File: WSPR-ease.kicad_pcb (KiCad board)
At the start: 4 copper layers, 100 x 75 mm, 98 parts, among them J101 GNSS Ant, J102 USB_C_16P_Stacked, J103 Tx Ant, Q101 MMBF170, Q102 MMBF170, Q103 MMBF170, Q104 MMBF170, Q105 MMBF170, Q106 MMBF170, Q107 MMBF170, Q108 MMBF170, Q109 MMBF170, Q110 MMBF170, Q111 MMBF170, Q112 MMBF170, SW101 BOOTSEL, SW102 RESET, T101 BN-43-202_DualPri_CTSec, U101 W25Q128JVS, U102 RP2040, U103 CD74AC244M, U104 ATGM336H-5N31, U105 NCP1117-3.3_SOT223, Y101 ABM8-272-T3

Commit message: Starting layout a bit
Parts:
- removed AE101: GPS_Patch_25mm, Library:gnss-antenna
- removed Q102, Q103, Q104, Q105, Q106, Q107, Q108, Q109, Q110, Q111, Q112: MMBF170, Package_TO_SOT_SMD:SOT-23
- removed R116, R120: 0, Resistor_SMD:R_0603_1608Metric
- removed R117, R118, R119: 10, Resistor_SMD:R_0603_1608Metric
- removed R121, R122, R125, R126: 100k, Resistor_SMD:R_0603_1608Metric
- removed R123, R124: 5.1k, Resistor_SMD:R_0603_1608Metric
- removed T101: BN-43-202_DualPri_CTSec, Library:bn-43-202-horizontal
- removed U105: NCP1117-3.3_SOT223, Package_TO_SOT_SMD:SOT-223-3_TabPin2
- added C301: 10uF, Capacitor_SMD:C_0805_2012Metric, F.Cu at (115.2, 80.7)
- added C302: 100nF, Capacitor_SMD:C_0603_1608Metric, F.Cu at (112.7, 78.7)
- added C401: 15pF, Capacitor_SMD:C_0603_1608Metric, F.Cu at (116.8, 116.7)
- added C402: 1uF, Capacitor_SMD:C_0603_1608Metric, F.Cu at (109.8, 126.9)
- added C403: 15pF, Capacitor_SMD:C_0603_1608Metric, F.Cu at (116.8, 112.2)
- added C404: 1uF, Capacitor_SMD:C_0603_1608Metric, F.Cu at (114.6, 122.1)
- added C405: 100nF, Capacitor_SMD:C_0603_1608Metric, F.Cu at (114.6, 118.9)
- added C406: 100nF, Capacitor_SMD:C_0603_1608Metric, F.Cu at (106.8, 121.4)
- added C407: 100nF, Capacitor_SMD:C_0603_1608Metric, F.Cu at (115.3, 116.6)
- added C410: 100nF, Capacitor_SMD:C_0603_1608Metric, F.Cu at (103.6, 118.9)
- added C411: 10nF, Capacitor_SMD:C_0603_1608Metric, F.Cu at (110.8, 122.1)
- added C412: 100nF, Capacitor_SMD:C_0603_1608Metric, F.Cu at (102.3, 113.4)
- added C413: 4.7uF, Capacitor_SMD:C_0603_1608Metric, F.Cu at (112.6, 121.7)
- added C414: 100nF, Capacitor_SMD:C_0603_1608Metric, F.Cu at (108.3, 121.4)
- added C417: 100nF, Capacitor_SMD:C_0603_1608Metric, F.Cu at (125.3, 123.7)
- added C418: 6.8nF, Capacitor_SMD:C_0603_1608Metric, F.Cu at (125.3, 119.1)
- added C419: 6.8nF, Capacitor_SMD:C_0603_1608Metric, F.Cu at (125.3, 120.9)
- added FB401: 120 @ 100MHz, Inductor_SMD:L_0805_2012Metric, F.Cu at (109.5, 129.9)
- added J104: Tx Ant, Connector_Coaxial:SMA_BAT_Wireless_BWSMA-KWE-Z001, F.Cu at (143.9, 64.4)
- added J401: RJ45_Hanrun_HR911105A_Horizontal, Connector_RJ:RJ45_Hanrun_HR911105A_Horizontal, F.Cu at (131.6, 126.5)
- added Q301: MMBF170, Package_TO_SOT_SMD:SOT-23, F.Cu at (121.0, 70.6)
- added Q302: MMBF170, Package_TO_SOT_SMD:SOT-23, F.Cu at (124.5, 70.6)
- added Q303: MMBF170, Package_TO_SOT_SMD:SOT-23, F.Cu at (128.0, 70.6)
- added Q304: MMBF170, Package_TO_SOT_SMD:SOT-23, F.Cu at (128.1, 65.5)
- added Q305: MMBF170, Package_TO_SOT_SMD:SOT-23, F.Cu at (124.6, 65.5)
- added Q306: MMBF170, Package_TO_SOT_SMD:SOT-23, F.Cu at (121.1, 65.5)
- added Q307: MMBF170, Package_TO_SOT_SMD:SOT-23, F.Cu at (96.1, 65.3)
- added Q308: MMBF170, Package_TO_SOT_SMD:SOT-23, F.Cu at (92.7, 65.3)
- added Q309: MMBF170, Package_TO_SOT_SMD:SOT-23, F.Cu at (89.1, 65.3)
- added Q310: MMBF170, Package_TO_SOT_SMD:SOT-23, F.Cu at (89.0, 70.5)
- added Q311: MMBF170, Package_TO_SOT_SMD:SOT-23, F.Cu at (92.3, 70.5)
- added Q312: MMBF170, Package_TO_SOT_SMD:SOT-23, F.Cu at (95.8, 70.5)
- added R301: 10, Resistor_SMD:R_0603_1608Metric, F.Cu at (120.0, 74.2)
- added R302: 10, Resistor_SMD:R_0603_1608Metric, F.Cu at (123.5, 74.2)
- added R303: 10, Resistor_SMD:R_0603_1608Metric, F.Cu at (127.0, 74.2)
- added R304: 10, Resistor_SMD:R_0603_1608Metric, F.Cu at (129.1, 61.8)
- added R305: 10, Resistor_SMD:R_0603_1608Metric, F.Cu at (125.6, 61.8)
- added R306: 10, Resistor_SMD:R_0603_1608Metric, F.Cu at (122.1, 61.8)
- added R307: 10, Resistor_SMD:R_0603_1608Metric, F.Cu at (96.8, 61.9)
- added R308: 10, Resistor_SMD:R_0603_1608Metric, F.Cu at (93.6, 61.9)
- added R309: 10, Resistor_SMD:R_0603_1608Metric, F.Cu at (90.1, 61.9)
- added R310: 10, Resistor_SMD:R_0603_1608Metric, F.Cu at (88.1, 74.2)
- added R311: 10, Resistor_SMD:R_0603_1608Metric, F.Cu at (91.6, 74.2)
- added R312: 10, Resistor_SMD:R_0603_1608Metric, F.Cu at (94.8, 74.2)
- added R401: 0, Resistor_SMD:R_0603_1608Metric, F.Cu at (116.0, 114.4)
- added R402: 1M, Resistor_SMD:R_0603_1608Metric, F.Cu at (118.3, 114.5)
- added R403: 10k, Resistor_SMD:R_0603_1608Metric, F.Cu at (117.7, 105.7)
- added R404: 10k, Resistor_SMD:R_0603_1608Metric, F.Cu at (108.7, 105.7)
- added R405: 10k, Resistor_SMD:R_0603_1608Metric, F.Cu at (116.2, 105.7)
- added R406: 10k, Resistor_SMD:R_0603_1608Metric, F.Cu at (114.7, 105.7)
- added R407: 10k, Resistor_SMD:R_0603_1608Metric, F.Cu at (107.1, 105.7)
- added R408: 10k, Resistor_SMD:R_0603_1608Metric, F.Cu at (113.2, 105.7)
- added R409: 10k, Resistor_SMD:R_0603_1608Metric, F.Cu at (105.7, 105.7)
- added R410: 10k, Resistor_SMD:R_0603_1608Metric, F.Cu at (111.7, 105.7)
- added R411: 10k, Resistor_SMD:R_0603_1608Metric, F.Cu at (110.1, 105.7)
- added R412: 12.4k, Resistor_SMD:R_0603_1608Metric, F.Cu at (100.3, 116.4)
- added R413: 3.3, Resistor_SMD:R_0603_1608Metric, F.Cu at (125.5, 126.7)
- added R414: 3.3, Resistor_SMD:R_0603_1608Metric, F.Cu at (122.3, 119.1)
- added R415: 49.9, Resistor_SMD:R_0603_1608Metric, F.Cu at (125.0, 125.2)
- added R416: 49.9, Resistor_SMD:R_0603_1608Metric, F.Cu at (122.0, 117.6)
- added R417: 49.9, Resistor_SMD:R_0603_1608Metric, F.Cu at (125.0, 129.7)
- added R418: 49.9, Resistor_SMD:R_0603_1608Metric, F.Cu at (122.0, 122.4)
- added R419: 3.3, Resistor_SMD:R_0603_1608Metric, F.Cu at (125.5, 128.2)
- added R420: 3.3, Resistor_SMD:R_0603_1608Metric, F.Cu at (122.3, 120.9)
- added R421: 1k, Resistor_SMD:R_0603_1608Metric, F.Cu at (142.6, 131.9)
- added R422: 1k, Resistor_SMD:R_0603_1608Metric, F.Cu at (138.5, 131.9)
- added T301: BN-43-202_DualPri_CTSec, Library:bn-43-202-horizontal, F.Cu at (108.3, 68.4)
- added U301: CD74AC244M, Library:DW20, F.Cu at (107.2, 86.3)
- added U401: LP5907MFX-3.3, Package_TO_SOT_SMD:SOT-23-5, F.Cu at (113.5, 127.8)
- added U402: W5500, Package_QFP:LQFP-48_7x7mm_P0.5mm, F.Cu at (109.1, 114.8)
- added Y401: 25MHz, Crystal:Crystal_SMD_Abracon_ABM8G-4Pin_3.2x2.5mm, F.Cu at (121.0, 114.3)
- C107: footprint Capacitor_SMD:C_0805_2012Metric -> Capacitor_SMD:C_0603_1608Metric
- C110: value 100nF -> 1uF
- C111: value 1uF -> 100nF
- C113, C115: value 100nF -> 10uF; footprint Capacitor_SMD:C_0603_1608Metric -> Capacitor_SMD:C_0805_2012Metric
- C114: footprint Capacitor_SMD:C_0603_1608Metric -> Capacitor_SMD:C_0805_2012Metric
- C116, C120, C122: value 10uF -> 100nF; footprint Capacitor_SMD:C_0805_2012Metric -> Capacitor_SMD:C_0603_1608Metric
- C119: value 100pF NP0 -> 10uF; footprint Capacitor_SMD:C_0603_1608Metric -> Capacitor_SMD:C_0805_2012Metric
- C121: value 100nF -> 100pF NP0
- J101: value GNSS Ant -> DEBUG; footprint Connector_Coaxial:SMA_BAT_Wireless_BWSMA-KWE-Z001 -> Connector:Tag-Connect_TC2030-IDC-NL_2x03_P1.27mm_Vertical
- J102: value USB_C_16P_Stacked -> GNSS Ant; footprint Library:HRO-TYPE-C-31-M-12 -> Connector_Coaxial:SMA_BAT_Wireless_BWSMA-KWE-Z001
- J103: value Tx Ant -> USB_C_16P_Stacked; footprint Connector_Coaxial:SMA_BAT_Wireless_BWSMA-KWE-Z001 -> Library:HRO-TYPE-C-31-M-12
- Q101: value MMBF170 -> 2N7002
- R101, R106: value 10k -> 100k
- R102, R105: value 1k -> 100k
- R103: value 27 -> 10k
- R104: value 27 -> 1k
- R107, R108: value 10 -> 27
- R109: value 10 -> 1k
- R110: value 10 -> 200
- R111: value 10 -> 10k
- R112: value 10 -> 200k
- R113: value 10 -> 100k
- R114, R115: value 10 -> 5.1k
- U103: value CD74AC244M -> NCP1117-3.3_SOT223; footprint Library:DW20 -> Package_TO_SOT_SMD:SOT-223-3_TabPin2
- Y101: value ABM8-272-T3 -> 12MHz
- moved J103 78.2 mm to (49.6, 122.7), turned to 90 degrees
- moved U104 72.0 mm to (67.7, 91.9)
- moved C119 70.5 mm to (55.1, 112.2), turned to 180 degrees
- moved L101 68.0 mm to (59.8, 97.4), turned to 180 degrees
- moved R114 64.9 mm to (57.6, 123.9), turned to 0 degrees
- moved R115 64.5 mm to (57.5, 120.9), turned to 0 degrees
- moved C116 54.9 mm to (79.3, 121.2), turned to 180 degrees
- moved BT101 53.5 mm to (75.8, 89.8), turned to -90 degrees
- moved C107 49.5 mm to (89.6, 132.7), turned to 180 degrees
- moved R113 49.5 mm to (71.6, 113.9), turned to -90 degrees
- moved C203 49.2 mm to (144.9, 86.4), turned to 0 degrees
- moved R106 49.2 mm to (86.1, 131.4), turned to -90 degrees
- moved C211 47.9 mm to (147.8, 80.7), turned to -90 degrees
- moved S201 46.2 mm to (136.9, 90.9), turned to -90 degrees
- moved L203 46.1 mm to (144.2, 83.9), turned to 90 degrees
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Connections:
- C107 pad 1: GND -> +3.3V
- C107 pad 2: +3.3V -> GND
- C109 pad 1: GND -> +3.3V
- C109 pad 2: +3.3V -> GND
- C110 pad 1: +3.3V -> Net-(U102-VREG_IN)
- C114 pad 1: +3.3V -> Net-(Q101-S)
- C115 pad 1: +3.3V -> VBUS
- C119 pad 1: Net-(C119-Pad1) -> +3.3V
- C119 pad 2: Net-(J101-In) -> GND
- C120 pad 1: VBUS -> +3.3V
- C121 pad 1: VBUS -> Net-(U104-RF_IN)
- C121 pad 2: GND -> Net-(J102-In)
- C123 pad 1: +3.3V -> VBUS
- J101 pad 1: Net-(J101-In) -> +3.3V
- J101 pad 2: GND -> /SWD
- L101 pad 2: Net-(J101-In) -> Net-(J102-In)
- Q101 pad 1: Net-(Q101-G) -> +3.3V
- Q101 pad 2: GND -> Net-(Q101-S)
- R101 pad 1: +3.3V -> /hiON
- R101 pad 2: Net-(U102-RUN) -> GND
- R102 pad 1: Net-(R102-Pad1) -> /loON
- R102 pad 2: /qsSS -> GND
- R103 pad 1: /D+ -> +3.3V
- R103 pad 2: Net-(U102-USB_DP) -> /nRESET
- R104 pad 1: /D- -> Net-(R104-Pad1)
- R104 pad 2: Net-(U102-USB_DM) -> /qsSS
- R105 pad 1: Net-(C102-Pad2) -> /lo1ON
- R105 pad 2: Net-(U102-XOUT) -> GND
- R106 pad 1: Net-(U102-GPIO14) -> /lo2ON
- R106 pad 2: /gnssPPS -> GND
- R107 pad 1: Net-(U103-1Y0) -> /D+
- R107 pad 2: Net-(Q101-G) -> Net-(U102-USB_DP)
- R108 pad 1: Net-(U103-1Y0) -> /D-
- R108 pad 2: Net-(Q102-G) -> Net-(U102-USB_DM)
- R109 pad 1: Net-(U103-1Y0) -> Net-(C102-Pad2)
- R109 pad 2: Net-(Q103-G) -> Net-(U102-XOUT)
- R110 pad 1: Net-(U103-1Y2) -> +3.3V
- R110 pad 2: Net-(Q104-G) -> Net-(U102-ADC_AVDD)
- R111 pad 1: Net-(U103-1Y2) -> Net-(U102-GPIO14)
- R111 pad 2: Net-(Q105-G) -> /gnssPPS
- R112 pad 1: Net-(U103-1Y2) -> VBUS
- R112 pad 2: Net-(Q106-G) -> Net-(Q101-S)
- R113 pad 1: Net-(U103-2Y0) -> Net-(Q101-S)
- R113 pad 2: Net-(Q107-G) -> GND
- R114 pad 1: Net-(U103-2Y0) -> Net-(J103-CC1)
- R114 pad 2: Net-(Q108-G) -> GND
- R115 pad 1: Net-(U103-2Y0) -> Net-(J103-CC2)
- R115 pad 2: Net-(Q109-G) -> GND
- SW101 pad 2: Net-(R102-Pad1) -> Net-(R104-Pad1)
- SW102 pad 2: Net-(U102-RUN) -> /nRESET
- U102 pad 24: unconnected-(U102-SWCLK-Pad24) -> /SWCLK
- U102 pad 25: unconnected-(U102-SWD-Pad25) -> /SWD
- U102 pad 26: Net-(U102-RUN) -> /nRESET
- U102 pad 27: unconnected-(U102-GPIO16-Pad27) -> /ethMISO
- U102 pad 28: unconnected-(U102-GPIO17-Pad28) -> /ethNCS
- U102 pad 29: unconnected-(U102-GPIO18-Pad29) -> /ethSCLK
- U102 pad 30: unconnected-(U102-GPIO19-Pad30) -> /ethMOSI
- U102 pad 31: unconnected-(U102-GPIO20-Pad31) -> /ethNIRQ
- U102 pad 32: unconnected-(U102-GPIO21-Pad32) -> /ethRESET
- U102 pad 41: unconnected-(U102-GPIO29_ADC3-Pad41) -> Net-(Q101-D)
- U102 pad 43: +3.3V -> Net-(U102-ADC_AVDD)
- U102 pad 44: +3.3V -> Net-(U102-VREG_IN)
- U103 pad 2: /push1 -> +3.3V
- U103 pad 3: Net-(U103-2Y2) -> VBUS
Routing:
- added copper zone on In2.Cu, net +3.3V
- added copper zone on In1.Cu, net GND
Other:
- board text added: "*"

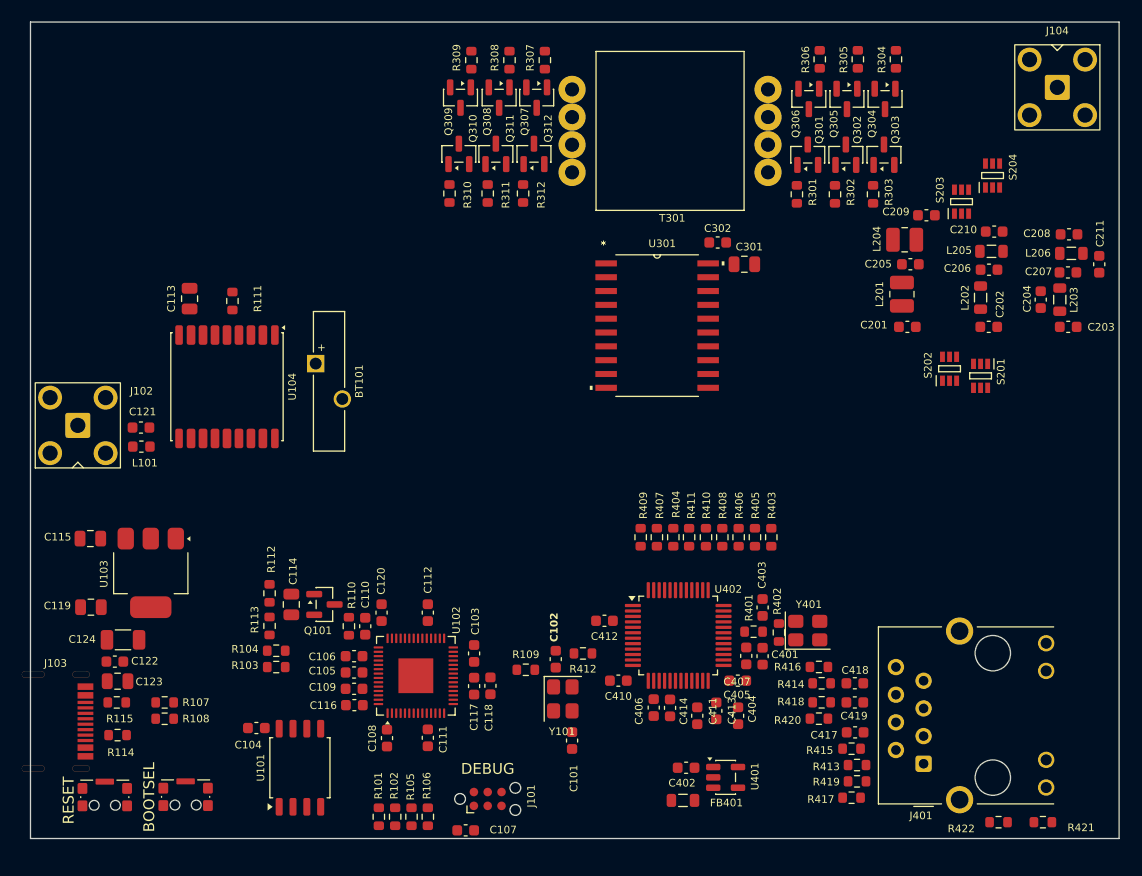
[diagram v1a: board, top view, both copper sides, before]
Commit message: Well it is routed and passes DRC
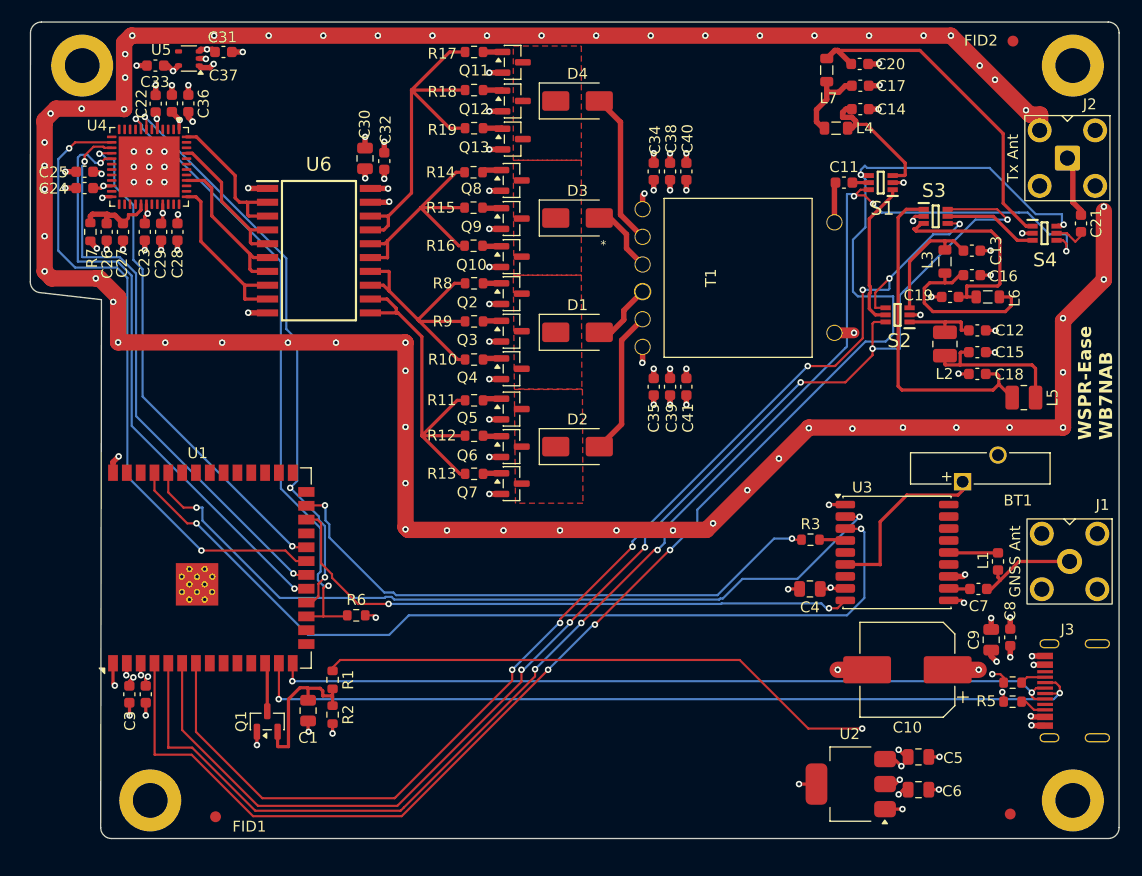
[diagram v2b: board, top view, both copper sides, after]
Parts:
- removed BT101: CR1220, Battery:Battery_Panasonic_CR1220-VCN_Vertical_CircularHoles
- removed C101, C102, C208: 15pF NP0, Capacitor_SMD:C_0603_1608Metric
- removed C103, C104, C105, C108, C109, C111, C112, C116, C117, C118, C120, C122, C302, C405, C406, C407, C410, C412, C414, C417: 100nF, Capacitor_SMD:C_0603_1608Metric
- removed C106, C110, C402, C404: 1uF, Capacitor_SMD:C_0603_1608Metric
- removed C107: 10uF, Capacitor_SMD:C_0603_1608Metric
- removed C113, C115, C119, C123, C301: 10uF, Capacitor_SMD:C_0805_2012Metric
- removed C114: 100nF, Capacitor_SMD:C_0805_2012Metric
- removed C121: 100pF NP0, Capacitor_SMD:C_0603_1608Metric
- removed C124: 100uF, Capacitor_SMD:C_1206_3216Metric
- removed C201, C209: 1nF NP0, Capacitor_SMD:C_0603_1608Metric
- removed C202, C210: 330pF NP0, Capacitor_SMD:C_0603_1608Metric
- removed C203, C211: 120pF NP0, Capacitor_SMD:C_0603_1608Metric
- removed C204: 33pF NP0, Capacitor_SMD:C_0603_1608Metric
- removed C205: 1.8nF NP0, Capacitor_SMD:C_0603_1608Metric
- removed C206: 560pF NP0, Capacitor_SMD:C_0603_1608Metric
- removed C207: 270pF NP0, Capacitor_SMD:C_0603_1608Metric
- removed C401, C403: 15pF, Capacitor_SMD:C_0603_1608Metric
- removed C411: 10nF, Capacitor_SMD:C_0603_1608Metric
- removed C413: 4.7uF, Capacitor_SMD:C_0603_1608Metric
- removed C418, C419: 6.8nF, Capacitor_SMD:C_0603_1608Metric
- removed FB401: 120 @ 100MHz, Inductor_SMD:L_0805_2012Metric
- removed J101: DEBUG, Connector:Tag-Connect_TC2030-IDC-NL_2x03_P1.27mm_Vertical
- removed J102: GNSS Ant, Connector_Coaxial:SMA_BAT_Wireless_BWSMA-KWE-Z001
- removed J103: USB_C_16P_Stacked, Library:HRO-TYPE-C-31-M-12
- removed J104: Tx Ant, Connector_Coaxial:SMA_BAT_Wireless_BWSMA-KWE-Z001
- removed J401: RJ45_Hanrun_HR911105A_Horizontal, Connector_RJ:RJ45_Hanrun_HR911105A_Horizontal
- removed L101: 47nH, Inductor_SMD:L_0603_1608Metric
- removed L201, L204: 2.2uH, Inductor_SMD:L_1008_2520Metric
- removed L202, L205: 390nH, Inductor_SMD:L_0805_2012Metric
- removed L203, L206: 270nH, Inductor_SMD:L_0805_2012Metric
- removed Q101: 2N7002, Package_TO_SOT_SMD:SOT-23
- removed Q301, Q302, Q303, Q304, Q305, Q306, Q307, Q308, Q309, Q310, Q311, Q312: MMBF170, Package_TO_SOT_SMD:SOT-23
- removed R101, R102, R105, R106, R113: 100k, Resistor_SMD:R_0603_1608Metric
- removed R103, R111, R403, R404, R405, R406, R407, R408, R409, R410, R411: 10k, Resistor_SMD:R_0603_1608Metric
- removed R104, R109, R421, R422: 1k, Resistor_SMD:R_0603_1608Metric
- removed R107, R108: 27, Resistor_SMD:R_0603_1608Metric
- removed R110: 200, Resistor_SMD:R_0603_1608Metric
- removed R112: 200k, Resistor_SMD:R_0603_1608Metric
- removed R114, R115: 5.1k, Resistor_SMD:R_0603_1608Metric
- removed R301, R302, R303, R304, R305, R306, R307, R308, R309, R310, R311, R312: 10, Resistor_SMD:R_0603_1608Metric
- removed R401: 0, Resistor_SMD:R_0603_1608Metric
- removed R402: 1M, Resistor_SMD:R_0603_1608Metric
- removed R412: 12.4k, Resistor_SMD:R_0603_1608Metric
- removed R413, R414, R419, R420: 3.3, Resistor_SMD:R_0603_1608Metric
- removed R415, R416, R417, R418: 49.9, Resistor_SMD:R_0603_1608Metric
- removed S201, S202, S203, S204: AS183-92LF, Library:SOT65P220X110-6N
- removed SW101: BOOTSEL, Button_Switch_SMD:SW_SPST_CK_KMS2xxGP
- removed SW102: RESET, Button_Switch_SMD:SW_SPST_CK_KMS2xxGP
- removed T301: BN-43-202_DualPri_CTSec, Library:bn-43-202-horizontal
- removed U101: W25Q128JVS, Package_SO:SOIC-8_5.3x5.3mm_P1.27mm
- removed U102: RP2040, Package_DFN_QFN:QFN-56-1EP_7x7mm_P0.4mm_EP3.2x3.2mm
- removed U103: NCP1117-3.3_SOT223, Package_TO_SOT_SMD:SOT-223-3_TabPin2
- removed U104: ATGM336H-5N31, RF_GPS:ublox_MAX
- removed U301: CD74AC244M, Library:DW20
- removed U401: LP5907MFX-3.3, Package_TO_SOT_SMD:SOT-23-5
- removed U402: W5500, Package_QFP:LQFP-48_7x7mm_P0.5mm
- removed Y101: 12MHz, Crystal:Crystal_SMD_Abracon_ABM8G-4Pin_3.2x2.5mm
- removed Y401: 25MHz, Crystal:Crystal_SMD_Abracon_ABM8G-4Pin_3.2x2.5mm
- added BT1: CR1220, Battery:Battery_Panasonic_CR1220-VCN_Vertical_CircularHoles, F.Cu at (135.2, 100.6)
- added C1: 100nF, Capacitor_SMD:C_0805_2012Metric, F.Cu at (75.1, 121.7)
- added C10: 100uF, Capacitor_SMD:CP_Elec_8x10.5, F.Cu at (130.2, 117.9)
- added C11: 100nF, Capacitor_SMD:C_0603_1608Metric, F.Cu at (124.3, 73.2)
- added C12: 470pF, Capacitor_SMD:C_0603_1608Metric, F.Cu at (136.6, 86.7)
- added C13: 220pF, Capacitor_SMD:C_0603_1608Metric, F.Cu at (136.1, 79.4)
- added C14: 100pF, Capacitor_SMD:C_0603_1608Metric, F.Cu at (125.8, 66.4)
- added C15: 1nF, Capacitor_SMD:C_0603_1608Metric, F.Cu at (136.6, 88.7)
- added C16: 470pF, Capacitor_SMD:C_0603_1608Metric, F.Cu at (136.1, 81.7)
- added C17: 220pF, Capacitor_SMD:C_0603_1608Metric, F.Cu at (125.8, 64.2)
- added C18: 470pF, Capacitor_SMD:C_0603_1608Metric, F.Cu at (136.6, 90.7)
- added C19: 220pF, Capacitor_SMD:C_0603_1608Metric, F.Cu at (134.1, 83.7)
- added C2: 0.1uF, Capacitor_SMD:C_0603_1608Metric, F.Cu at (60.2, 120.2)
- added C20: 100pF, Capacitor_SMD:C_0603_1608Metric, F.Cu at (125.8, 62.2)
- added C21: 100nF, Capacitor_SMD:C_0603_1608Metric, F.Cu at (146.1, 76.9)
- added C22: 0.1uF, Capacitor_SMD:C_0603_1608Metric, F.Cu at (61.1, 65.9)
- added C23: 10uF, Capacitor_SMD:C_0603_1608Metric, F.Cu at (60.1, 77.7)
- added C24: 0.1uF, Capacitor_SMD:C_0603_1608Metric, F.Cu at (54.6, 73.7)
- added C25: 10uF, Capacitor_SMD:C_0603_1608Metric, F.Cu at (54.6, 72.2)
- added C26: 0.1uF, Capacitor_SMD:C_0603_1608Metric, F.Cu at (56.6, 77.7)
- added C27: 10uF, Capacitor_SMD:C_0603_1608Metric, F.Cu at (58.1, 77.7)
- added C28: 0.1uF, Capacitor_SMD:C_0603_1608Metric, F.Cu at (63.1, 77.7)
- added C29: 10uF, Capacitor_SMD:C_0603_1608Metric, F.Cu at (61.6, 77.7)
- added C3: 22uF, Capacitor_SMD:C_0603_1608Metric, F.Cu at (58.7, 120.2)
- added C30: 10uF, Capacitor_SMD:C_0805_2012Metric, F.Cu at (80.3, 70.9)
- added C31: 1uF, Capacitor_SMD:C_0603_1608Metric, F.Cu at (67.3, 61.1)
- added C32: 0.1uF, Capacitor_SMD:C_0603_1608Metric, F.Cu at (82.1, 71.2)
- added C33: 1uF, Capacitor_SMD:C_0603_1608Metric, F.Cu at (61.1, 62.4)
- added C34: 10uF X7R, Capacitor_SMD:C_0603_1608Metric, F.Cu at (106.8, 72.1)
- added C35: 10uF X7R, Capacitor_SMD:C_0603_1608Metric, F.Cu at (106.8, 91.9)
- added C36: 0.1uF, Capacitor_SMD:C_0603_1608Metric, F.Cu at (64.1, 65.9)
- added C37: 10uF, Capacitor_SMD:C_0603_1608Metric, F.Cu at (62.6, 65.9)
- added C38: 0.1uF X7R, Capacitor_SMD:C_0603_1608Metric, F.Cu at (108.3, 72.1)
- added C39: 0.1uF X7R, Capacitor_SMD:C_0603_1608Metric, F.Cu at (108.3, 91.9)
- added C4: 10uF, Capacitor_SMD:C_0805_2012Metric, F.Cu at (121.2, 110.5)
- added C40: 100pF NP0 50V, Capacitor_SMD:C_0603_1608Metric, F.Cu at (109.8, 72.1)
- added C41: 100pF NP0 50V, Capacitor_SMD:C_0603_1608Metric, F.Cu at (109.8, 91.9)
- added C5: 10uF, Capacitor_SMD:C_0805_2012Metric, F.Cu at (131.2, 125.9)
- added C6: 10uF, Capacitor_SMD:C_0805_2012Metric, F.Cu at (131.2, 128.9)
- added C7: 100pF NP0, Capacitor_SMD:C_0603_1608Metric, F.Cu at (136.7, 110.5)
- added C8: 100nF, Capacitor_SMD:C_0603_1608Metric, F.Cu at (139.6, 114.9)
- added C9: 10uF, Capacitor_SMD:C_0805_2012Metric, F.Cu at (137.8, 115.1)
- added D1: SS14, Diode_SMD:D_SMA, F.Cu at (99.8, 86.9)
- added D2: SS14, Diode_SMD:D_SMA, F.Cu at (99.8, 97.4)
- added D3: SS14, Diode_SMD:D_SMA, F.Cu at (99.8, 76.4)
- added D4: SS14, Diode_SMD:D_SMA, F.Cu at (99.8, 65.7)
- added FID1: Fiducial, Fiducial:Fiducial_1mm_Mask2mm, F.Cu at (66.6, 131.4)
- added FID2: Fiducial, Fiducial:Fiducial_1mm_Mask2mm, F.Cu at (139.8, 60.1)
- added FID3: Fiducial, Fiducial:Fiducial_1mm_Mask2mm, F.Cu at (139.6, 131.2)
- added H1: MountingHole_Pad, MountingHole:MountingHole_3.2mm_M3_ISO7380_Pad, F.Cu at (60.6, 129.9)
- added H2: MountingHole_Pad, MountingHole:MountingHole_3.2mm_M3_ISO7380_Pad, F.Cu at (145.3, 62.4)
- added H3: MountingHole_Pad, MountingHole:MountingHole_3.2mm_M3_ISO7380_Pad, F.Cu at (54.4, 62.4)
- added H4: MountingHole_Pad, MountingHole:MountingHole_3.2mm_M3_ISO7380_Pad, F.Cu at (145.3, 129.9)
- added J1: GNSS Ant, Connector_Coaxial:SMA_BAT_Wireless_BWSMA-KWE-Z001, F.Cu at (145.1, 108.0)
- added J2: Tx Ant, Connector_Coaxial:SMA_BAT_Wireless_BWSMA-KWE-Z001, F.Cu at (144.8, 70.9)
- added J3: USB_C_16P_Stacked, Library:HRO-TYPE-C-31-M-12, F.Cu at (147.8, 119.8)
- added L1: 47nH, Inductor_SMD:L_0603_1608Metric, F.Cu at (138.5, 108.0)
- added L2: 1.2uH, Inductor_SMD:L_1008_2520Metric, F.Cu at (133.6, 88.0)
- added L3: 560nH, Inductor_SMD:L_0805_2012Metric, F.Cu at (133.6, 80.4)
- added L4: 270nH, Inductor_SMD:L_0805_2012Metric, F.Cu at (123.6, 68.2)
- added L5: 1.2uH, Inductor_SMD:L_1008_2520Metric, F.Cu at (140.8, 92.9)
- added L6: 560nH, Inductor_SMD:L_0805_2012Metric, F.Cu at (137.5, 83.7)
- added L7: 270nH, Inductor_SMD:L_0805_2012Metric, F.Cu at (122.7, 62.8)
- added Q1: MMBF170, Package_TO_SOT_SMD:SOT-23, F.Cu at (71.3, 122.7)
- added Q10: MMBF170, Package_TO_SOT_SMD:SOT-23, F.Cu at (93.8, 80.0)
- added Q11: MMBF170, Package_TO_SOT_SMD:SOT-23, F.Cu at (93.9, 62.1)
- added Q12: MMBF170, Package_TO_SOT_SMD:SOT-23, F.Cu at (93.9, 65.7)
- added Q13: MMBF170, Package_TO_SOT_SMD:SOT-23, F.Cu at (93.9, 69.2)
- added Q2: MMBF170, Package_TO_SOT_SMD:SOT-23, F.Cu at (93.8, 83.3)
- added Q3: MMBF170, Package_TO_SOT_SMD:SOT-23, F.Cu at (93.8, 86.8)
- added Q4: MMBF170, Package_TO_SOT_SMD:SOT-23, F.Cu at (93.8, 90.2)
- added Q5: MMBF170, Package_TO_SOT_SMD:SOT-23, F.Cu at (93.8, 94.0)
- added Q6: MMBF170, Package_TO_SOT_SMD:SOT-23, F.Cu at (93.8, 97.4)
- added Q7: MMBF170, Package_TO_SOT_SMD:SOT-23, F.Cu at (93.8, 100.8)
- added Q8: MMBF170, Package_TO_SOT_SMD:SOT-23, F.Cu at (93.8, 73.0)
- added Q9: MMBF170, Package_TO_SOT_SMD:SOT-23, F.Cu at (93.8, 76.5)
- added R1: 100k, Resistor_SMD:R_0603_1608Metric, F.Cu at (77.3, 118.8)
- added R10: 10, Resistor_SMD:R_0603_1608Metric, F.Cu at (90.3, 89.4)
- added R11: 10, Resistor_SMD:R_0603_1608Metric, F.Cu at (90.3, 93.2)
- added R12: 10, Resistor_SMD:R_0603_1608Metric, F.Cu at (90.3, 96.4)
- added R13: 10, Resistor_SMD:R_0603_1608Metric, F.Cu at (90.3, 99.9)
- added R14: 10, Resistor_SMD:R_0603_1608Metric, F.Cu at (90.3, 72.2)
- added R15: 10, Resistor_SMD:R_0603_1608Metric, F.Cu at (90.3, 75.5)
- added R16: 10, Resistor_SMD:R_0603_1608Metric, F.Cu at (90.3, 79.0)
- added R17: 10, Resistor_SMD:R_0603_1608Metric, F.Cu at (90.3, 61.1)
- added R18: 10, Resistor_SMD:R_0603_1608Metric, F.Cu at (90.3, 64.7)
- added R19: 10, Resistor_SMD:R_0603_1608Metric, F.Cu at (90.3, 68.2)
- added R2: 100k, Resistor_SMD:R_0603_1608Metric, F.Cu at (77.3, 122.0)
- added R3: 10k, Resistor_SMD:R_0603_1608Metric, F.Cu at (121.2, 106.0)
- added R4: 5.1k, Resistor_SMD:R_0603_1608Metric, F.Cu at (139.8, 119.1)
- added R5: 5.1k, Resistor_SMD:R_0603_1608Metric, F.Cu at (139.8, 120.8)
- added R6: 10k, Resistor_SMD:R_0603_1608Metric, F.Cu at (79.5, 112.9)
- added R7: 10, Resistor_SMD:R_0603_1608Metric, F.Cu at (55.1, 77.7)
- added R8: 10, Resistor_SMD:R_0603_1608Metric, F.Cu at (90.3, 82.4)
- added R9: 10, Resistor_SMD:R_0603_1608Metric, F.Cu at (90.3, 85.9)
- added S1: AS183-92LF, Library:SOT65P220X110-6N, F.Cu at (127.7, 73.2)
- added S2: AS183-92LF, Library:SOT65P220X110-6N, F.Cu at (129.2, 85.3)
- added S3: AS183-92LF, Library:SOT65P220X110-6N, F.Cu at (132.8, 76.2)
- added S4: AS183-92LF, Library:SOT65P220X110-6N, F.Cu at (142.8, 77.8)
- added T1: BN-43-202_DualPri_CTSec, Library:bn-43-202-horizontal, F.Cu at (114.6, 81.9)
- added U1: ESP32-S3-WROOM-1, Library:ESP32-S3-WROOM-1, F.Cu at (62.4, 108.5)
- added U2: NCP1117-3.3_SOT223, Package_TO_SOT_SMD:SOT-223-3_TabPin2, F.Cu at (125.0, 128.4)
- added U3: ATGM336H-5N31, RF_GPS:ublox_MAX, F.Cu at (129.2, 107.1)
- added U4: ICE40UP5K-SG48ITR, Package_DFN_QFN:QFN-48-1EP_7x7mm_P0.5mm_EP5.6x5.6mm, F.Cu at (60.5, 71.7)
- added U5: TLV70012, Package_TO_SOT_SMD:SOT-353_SC-70-5, F.Cu at (64.2, 61.8)
- added U6: CD74ACT541M96G4, Library:SOIC127P1030X265-20N, F.Cu at (76.1, 79.4)
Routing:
- net GND: track 0.00 -> 338.3 mm, vias 0 -> 139
- net /hiON: track 0.00 -> 139.9 mm, vias 0 -> 5
- net /loON: track 0.00 -> 132.1 mm, vias 0 -> 6
- net /lo1ON: track 0.00 -> 121.0 mm, vias 0 -> 6
- net /lo2ON: track 0.00 -> 110.6 mm, vias 0 -> 7
- net /gnssRx: track 0.00 -> 81.7 mm, vias 0 -> 2
- net /D-: track 0.00 -> 78.8 mm, vias 0 -> 2
- net /gnssTx: track 0.00 -> 74.6 mm, vias 0 -> 2
- net VBUS: track 0.00 -> 74.2 mm, vias 0 -> 18
- net /D+: track 0.00 -> 73.1 mm, vias 0 -> 2
- net /fpgaNRESET: track 0.00 -> 59.9 mm, vias 0 -> 2
- net /fpgaMISO: track 0.00 -> 59.2 mm, vias 0 -> 2
- net /gnssNRESET: track 0.00 -> 55.6 mm, vias 0 -> 2
- net /fpgaMOSI: track 0.00 -> 54.8 mm, vias 0 -> 2
- net /fpgaDONE: track 0.00 -> 54.4 mm, vias 0 -> 3
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- added copper zone on In2.Cu, net +1V2
- added copper zone on F.Cu, net /Transmitter/pull1D
- added copper zone on F.Cu, net /Transmitter/pull2D
- added copper zone on F.Cu, net /Transmitter/push1D
- added copper zone on F.Cu, net /Transmitter/push2D
- added copper zone on In2.Cu, net VBUS
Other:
- outline, holes or cut-outs redrawn
- board text added: "WSPR-Ease WB7NAB"

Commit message: Minor tweaks after submitting 001 build to pcbway
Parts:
- added R20: 10k, Resistor_SMD:R_0603_1608Metric, F.Cu at (67.3, 77.4)
- added R21: 10k, Resistor_SMD:R_0603_1608Metric, F.Cu at (70.8, 68.9)
- added R22: 10k, Resistor_SMD:R_0603_1608Metric, F.Cu at (65.8, 80.7)
- added R23: 10k, Resistor_SMD:R_0603_1608Metric, F.Cu at (65.8, 83.9)
- BT1: value CR1220 -> S8401-46; footprint Battery:Battery_Panasonic_CR1220-VCN_Vertical_CircularHoles -> Library:S8401-46
- C1: footprint Capacitor_SMD:C_0805_2012Metric -> Capacitor_SMD:C_0603_1608Metric
- moved BT1 39.5 mm to (105.8, 127.0), turned to 180 degrees
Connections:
- net Net-(D1-A) renamed /Transmitter/push1T
- net Net-(D2-A) renamed /Transmitter/push2T
- net Net-(D3-A) renamed /Transmitter/pull1T
- net Net-(D4-A) renamed /Transmitter/pull2T
- BT1 pad 1: Net-(BT1-+) -> GND
- BT1 pad 2: GND -> Net-(U3-V_BCKP)
- D3 pad 1: /Transmitter/pull2D -> /Transmitter/pull1D
- D4 pad 1: /Transmitter/pull1D -> /Transmitter/pull2D
- Q10 pad 3: /Transmitter/pull2D -> /Transmitter/pull1D
- Q11 pad 3: /Transmitter/pull1D -> /Transmitter/pull2D
- Q12 pad 3: /Transmitter/pull1D -> /Transmitter/pull2D
- Q13 pad 3: /Transmitter/pull1D -> /Transmitter/pull2D
- Q8 pad 3: /Transmitter/pull2D -> /Transmitter/pull1D
- Q9 pad 3: /Transmitter/pull2D -> /Transmitter/pull1D
- U3 pad 6: Net-(BT1-+) -> Net-(U3-V_BCKP)
- U4 pad 40: /Transmitter/push1 -> unconnected-(U4A-RGB1-Pad40)
- U4 pad 42: unconnected-(U4A-IOT_51a-Pad42) -> /Transmitter/push1
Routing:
- net Net-(U3-V_BCKP): track 0.00 -> 38.7 mm, vias 0 -> 2
- net Net-(BT1-+): track 16.7 -> 0.00 mm
- net GND: track 338.3 -> 343.5 mm, vias 139 -> 141
- net /Transmitter/push2: track 16.3 -> 21.0 mm
- net /Transmitter/push1: track 15.0 -> 18.6 mm
- net /Transmitter/pull2: track 14.2 -> 16.9 mm
- net /Transmitter/pull1: track 14.1 -> 16.0 mm
- net /loON: track 132.1 -> 131.0 mm
- net /hiON: track 139.9 -> 139.1 mm
- net /fpgaDONE: track 54.4 -> 53.7 mm, vias 3 -> 2
- net /gnssTx: track 74.6 -> 73.9 mm
- net Net-(U1-IO48): track 52.6 -> 51.9 mm
- net /Transmitter/pull2D: track 0.00 -> 0.07 mm, vias 0 -> 16
- net /Transmitter/pull1D: track 0.07 -> 0.00 mm, vias 0 -> 16
- net /Transmitter/push2D: vias 0 -> 16
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- added copper zone on B.Cu, net /Transmitter/pull1D
- added copper zone on B.Cu, net /Transmitter/pull2D
- added copper zone on B.Cu, net /Transmitter/push1D
- added copper zone on B.Cu, net /Transmitter/push2D
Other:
- board size 100 x 75 mm -> 99.2 x 74.8 mm
